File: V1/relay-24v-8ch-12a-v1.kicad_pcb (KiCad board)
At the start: 2 copper layers, 98 x 67.8 mm, 47 parts, among them J1 DB141V-2.54-2P, J2 DB141V-2.54-4P, J3 DB141V-2.54-4P, J4 DB142V-5.08-4P, J5 DB142V-5.08-4P, J6 DB142V-5.08-4P, J7 DB142V-5.08-4P, K1 G5PZ-1A, K2 G5PZ-1A, K3 G5PZ-1A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

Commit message: Review before fabrication
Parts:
- R1, R2, R3, R4, R5, R6, R7, R8: value 6k8/100mW -> 10k/100mW
- moved K1 10.8 mm to (132.0, 92.8)
- moved K2 10.8 mm to (144.0, 92.8)
- moved K3 10.8 mm to (156.0, 92.8)
- moved K4 10.8 mm to (168.0, 92.8)
- moved K5 10.8 mm to (180.0, 92.8)
- moved K6 10.8 mm to (192.0, 92.8)
- moved K7 10.8 mm to (204.0, 92.8)
- moved K8 10.8 mm to (216.0, 92.8)
- moved J4 8.50 mm to (136.8, 119.0)
- moved J5 8.50 mm to (160.8, 119.0)
- moved J6 8.50 mm to (184.8, 119.0)
- moved J7 8.50 mm to (208.8, 119.0)
- moved J2 4.65 mm to (168.2, 70.5)
- moved J3 4.65 mm to (216.2, 70.5)
- moved RV1 3.25 mm to (131.5, 108.2)
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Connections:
- net Net-(D1-A) renamed /LED1
- net Net-(D1-K) renamed /IN1
- net Net-(D10-A) renamed /IN5
- net Net-(D11-A) renamed /LED6
- net Net-(D11-K) renamed /IN6
- net Net-(D13-A) renamed /LED7
- net Net-(D13-K) renamed /IN7
- net Net-(D15-A) renamed /LED8
- net Net-(D15-K) renamed /IN8
- net Net-(D3-A) renamed /LED2
- net Net-(D3-K) renamed /IN2
- net Net-(D5-A) renamed /LED3
- net Net-(D5-K) renamed /IN3
- net Net-(D7-A) renamed /LED4
- net Net-(D7-K) renamed /IN4
- net Net-(D9-A) renamed /LED5
- net Net-(J4-Pin_1) renamed /OUT1PW
- net Net-(J4-Pin_2) renamed /OUT1LD
- net Net-(J4-Pin_3) renamed /OUT2PW
- net Net-(J4-Pin_4) renamed /OUT2LD
- net Net-(J5-Pin_1) renamed /OUT3PW
- net Net-(J5-Pin_2) renamed /OUT3LD
- net Net-(J5-Pin_3) renamed /OUT4PW
- net Net-(J5-Pin_4) renamed /OUT4LD
- net Net-(J6-Pin_1) renamed /OUT5PW
- net Net-(J6-Pin_2) renamed /OUT5LD
- net Net-(J6-Pin_3) renamed /OUT6PW
- net Net-(J6-Pin_4) renamed /OUT6LD
- net Net-(J7-Pin_1) renamed /OUT7PW
- net Net-(J7-Pin_2) renamed /OUT7LD
- net Net-(J7-Pin_3) renamed /OUT8PW
- net Net-(J7-Pin_4) renamed /OUT8LD
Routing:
- net +24V: track 248.4 -> 238.5 mm
- net /IN6: track 53.9 -> 51.0 mm
- net /IN3: track 45.2 -> 48.0 mm
- net /IN5: track 52.4 -> 54.4 mm
- net /IN1: track 51.6 -> 53.6 mm
- net /IN7: track 47.2 -> 49.1 mm
- net /IN2: track 51.9 -> 50.0 mm
- net /IN4: track 46.9 -> 48.3 mm
- net /OUT4PW: track 48.1 -> 49.1 mm
- net /OUT8PW: track 48.1 -> 49.1 mm
- net /OUT6PW: track 48.1 -> 49.1 mm
- net /OUT2PW: track 48.1 -> 49.1 mm
- net /IN8: track 48.9 -> 49.7 mm
- net /OUT7LD: track 42.4 -> 41.7 mm
- net /OUT3LD: track 42.4 -> 41.7 mm
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- added copper zone on F.Cu, net +24V
- removed copper zone on B.Cu, net +24V
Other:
- rule pad_to_mask_clearance: 0 -> 0.1

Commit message: Revising before manufacturing.
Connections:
- net /OUT1PW renamed /OUT1LN
- net /OUT2PW renamed /OUT2LN
- net /OUT3PW renamed /OUT3LN
- net /OUT4PW renamed /OUT4LN
- net /OUT5PW renamed /OUT5LN
- net /OUT6PW renamed /OUT6LN
- net /OUT7PW renamed /OUT7LN
- net /OUT8PW renamed /OUT8LN
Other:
- board text added: "LINE"
- board text removed: "V~"
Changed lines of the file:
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@@
 	(net 17 "/IN8")
 	(net 18 "/OUT1LD")
-	(net 19 "/OUT2PW")
+	(net 19 "/OUT2LN")
 	(net 20 "/OUT2LD")
-	(net 21 "/OUT1PW")
+	(net 21 "/OUT1LN")
 	(net 22 "/OUT3LD")
-	(net 23 "/OUT4PW")
+	(net 23 "/OUT4LN")
 	(net 24 "/OUT4LD")
-	(net 25 "/OUT3PW")
-	(net 26 "/OUT5PW")
+	(net 25 "/OUT3LN")
+	(net 26 "/OUT5LN")
 	(net 27 "/OUT6LD")
-	(net 28 "/OUT6PW")
+	(net 28 "/OUT6LN")
 	(net 29 "/OUT5LD")
-	(net 30 "/OUT7PW")
+	(net 30 "/OUT7LN")
 	(net 31 "/OUT8LD")
-	(net 32 "/OUT8PW")
+	(net 32 "/OUT8LN")
 	(net 33 "/OUT7LD")
 	(footprint "Tales:D_SOD-123"
@@
 			(layers "*.Cu" "*.Mask")
 			(remove_unused_layers no)
-			(net 23 "/OUT4PW")
+			(net 23 "/OUT4LN")
 			(pintype "passive")
 		)
@@
 			(layers "*.Cu" "*.Mask")
 			(remove_unused_layers no)
-			(net 21 "/OUT1PW")
+			(net 21 "/OUT1LN")
 			(pintype "passive")
 		)
@@
 			(layers "*.Cu" "*.Mask")
 			(remove_unused_layers no)
-			(net 28 "/OUT6PW")
+			(net 28 "/OUT6LN")
 			(pintype "passive")
 		)
@@
 			(layers "*.Cu" "*.Mask")
 			(remove_unused_layers no)
-			(net 26 "/OUT5PW")
+			(net 26 "/OUT5LN")
 			(pinfunction "Pin_1")
 			(pintype "passive")
@@
 			(layers "*.Cu" "*.Mask")
 			(remove_unused_layers no)
-			(net 26 "/OUT5PW")
+			(net 26 "/OUT5LN")
 			(pinfunction "Pin_1")
 			(pintype "passive")
@@
 			(layers "*.Cu" "*.Mask")
 			(remove_unused_layers no)
-			(net 28 "/OUT6PW")
+			(net 28 "/OUT6LN")
 			(pinfunction "Pin_3")
 			(pintype "passive")
@@
 			(layers "*.Cu" "*.Mask")
 			(remove_unused_layers no)
-			(net 28 "/OUT6PW")
+			(net 28 "/OUT6LN")
 			(pinfunction "Pin_3")
 			(pintype "passive")
@@
 			(layers "*.Cu" "*.Mask")
 			(remove_unused_layers no)
-			(net 30 "/OUT7PW")
+			(net 30 "/OUT7LN")
 			(pintype "passive")
 		)
@@
 			(layers "*.Cu" "*.Mask")
 			(remove_unused_layers no)
-			(net 28 "/OUT6PW")
+			(net 28 "/OUT6LN")
 			(pintype "passive")
 		)
@@
 			(layers "*.Cu" "*.Mask")
 			(remove_unused_layers no)
-			(net 32 "/OUT8PW")
+			(net 32 "/OUT8LN")
 			(pintype "passive")
 		)
@@
 			(layers "*.Cu" "*.Mask")
 			(remove_unused_layers no)
-			(net 25 "/OUT3PW")
+			(net 25 "/OUT3LN")
 			(pintype "passive")
 		)
@@
 			(layers "*.Cu" "*.Mask")
 			(remove_unused_layers no)
-			(net 26 "/OUT5PW")
+			(net 26 "/OUT5LN")
 			(pintype "passive")
 		)
@@
 			(layers "*.Cu" "*.Mask")
 			(remove_unused_layers no)
-			(net 23 "/OUT4PW")
+			(net 23 "/OUT4LN")
 			(pintype "passive")
 		)
@@
 			(layers "*.Cu" "*.Mask")
 			(remove_unused_layers no)
-			(net 19 "/OUT2PW")
+			(net 19 "/OUT2LN")
 			(pintype "passive")
 		)
@@
 			(layers "*.Cu" "*.Mask")
 			(remove_unused_layers no)
-			(net 32 "/OUT8PW")
+			(net 32 "/OUT8LN")
 			(pintype "passive")
 		)
@@
 			(layers "*.Cu" "*.Mask")
 			(remove_unused_layers no)
-			(net 19 "/OUT2PW")
+			(net 19 "/OUT2LN")
 			(pintype "passive")
 		)
@@
 			(layers "*.Cu" "*.Mask")
 			(remove_unused_layers no)
-			(net 30 "/OUT7PW")
+			(net 30 "/OUT7LN")
 			(pinfunction "Pin_1")
 			(pintype "passive")
@@
 			(layers "*.Cu" "*.Mask")
 			(remove_unused_layers no)
-			(net 30 "/OUT7PW")
+			(net 30 "/OUT7LN")
 			(pinfunction "Pin_1")
 			(pintype "passive")
@@
 			(layers "*.Cu" "*.Mask")
 			(remove_unused_layers no)
-			(net 32 "/OUT8PW")
+			(net 32 "/OUT8LN")
 			(pinfunction "Pin_3")
 			(pintype "passive")
@@
 			(layers "*.Cu" "*.Mask")
 			(remove_unused_layers no)
-			(net 32 "/OUT8PW")
+			(net 32 "/OUT8LN")
 			(pinfunction "Pin_3")
 			(pintype "passive")
@@
 			(layers "*.Cu" "*.Mask")
 			(remove_unused_layers no)
-			(net 21 "/OUT1PW")
+			(net 21 "/OUT1LN")
 			(pintype "passive")
 		)
@@
 			(layers "*.Cu" "*.Mask")
 			(remove_unused_layers no)
-			(net 21 "/OUT1PW")
+			(net 21 "/OUT1LN")
 			(pinfunction "Pin_1")
 			(pintype "passive")
@@
 			(layers "*.Cu" "*.Mask")
 			(remove_unused_layers no)
-			(net 21 "/OUT1PW")
+			(net 21 "/OUT1LN")
 			(pinfunction "Pin_1")
 			(pintype "passive")
@@
 			(layers "*.Cu" "*.Mask")
 			(remove_unused_layers no)
-			(net 19 "/OUT2PW")
+			(net 19 "/OUT2LN")
 			(pinfunction "Pin_3")
 			(pintype "passive")
@@
 			(layers "*.Cu" "*.Mask")
 			(remove_unused_layers no)
-			(net 19 "/OUT2PW")
+			(net 19 "/OUT2LN")
 			(pinfunction "Pin_3")
 			(pintype "passive")
@@
 			(layers "*.Cu" "*.Mask")
 			(remove_unused_layers no)
-			(net 25 "/OUT3PW")
+			(net 25 "/OUT3LN")
 			(pintype "passive")
 		)
@@
 			(layers "*.Cu" "*.Mask")
 			(remove_unused_layers no)
-			(net 25 "/OUT3PW")
+			(net 25 "/OUT3LN")
 			(pinfunction "Pin_1")
 			(pintype "passive")
@@
 			(layers "*.Cu" "*.Mask")
 			(remove_unused_layers no)
-			(net 25 "/OUT3PW")
+			(net 25 "/OUT3LN")
 			(pinfunction "Pin_1")
 			(pintype "passive")
@@
 			(layers "*.Cu" "*.Mask")
 			(remove_unused_layers no)
-			(net 23 "/OUT4PW")
+			(net 23 "/OUT4LN")
 			(pinfunction "Pin_3")
 			(pintype "passive")
@@
 			(layers "*.Cu" "*.Mask")
 			(remove_unused_layers no)
-			(net 23 "/OUT4PW")
+			(net 23 "/OUT4LN")
 			(pinfunction "Pin_3")
 			(pintype "passive")
@@
 			(layers "*.Cu" "*.Mask")
 			(remove_unused_layers no)
-			(net 26 "/OUT5PW")
+			(net 26 "/OUT5LN")
 			(pintype "passive")
 		)
@@
 			(layers "*.Cu" "*.Mask")
 			(remove_unused_layers no)
-			(net 30 "/OUT7PW")
+			(net 30 "/OUT7LN")
 			(pintype "passive")
 		)
@@
 		)
 	)
-	(gr_text "V~"
+	(gr_text "LINE"
 		(at 187.26 125.75 0)
 		(layer "F.SilkS")
@@
 		)
 	)
-	(gr_text "V~"
+	(gr_text "LINE"
 		(at 139.26 125.75 0)
 		(layer "F.SilkS")
@@
 		)
 	)
-	(gr_text "V~"
+	(gr_text "LINE"
 		(at 163.16 125.75 0)
 		(layer "F.SilkS")
@@
 		)
 	)
-	(gr_text "V~"
+	(gr_text "LINE"
 		(at 129.1 125.75 0)
 		(layer "F.SilkS")
@@
 		)
 	)
-	(gr_text "V~"
+	(gr_text "LINE"
 		(at 211.16 125.75 0)
 		(layer "F.SilkS")
@@
 		)
 	)
-	(gr_text "V~"
+	(gr_text "LINE"
 		(at 201 125.75 0)
 		(layer "F.SilkS")
@@
 		)
 	)
-	(gr_text "V~"
+	(gr_text "LINE"
 		(at 153 125.75 0)
 		(layer "F.SilkS")
@@
 		)
 	)
-	(gr_text "V~"
+	(gr_text "LINE"
 		(at 177.1 125.75 0)
 		(layer "F.SilkS")

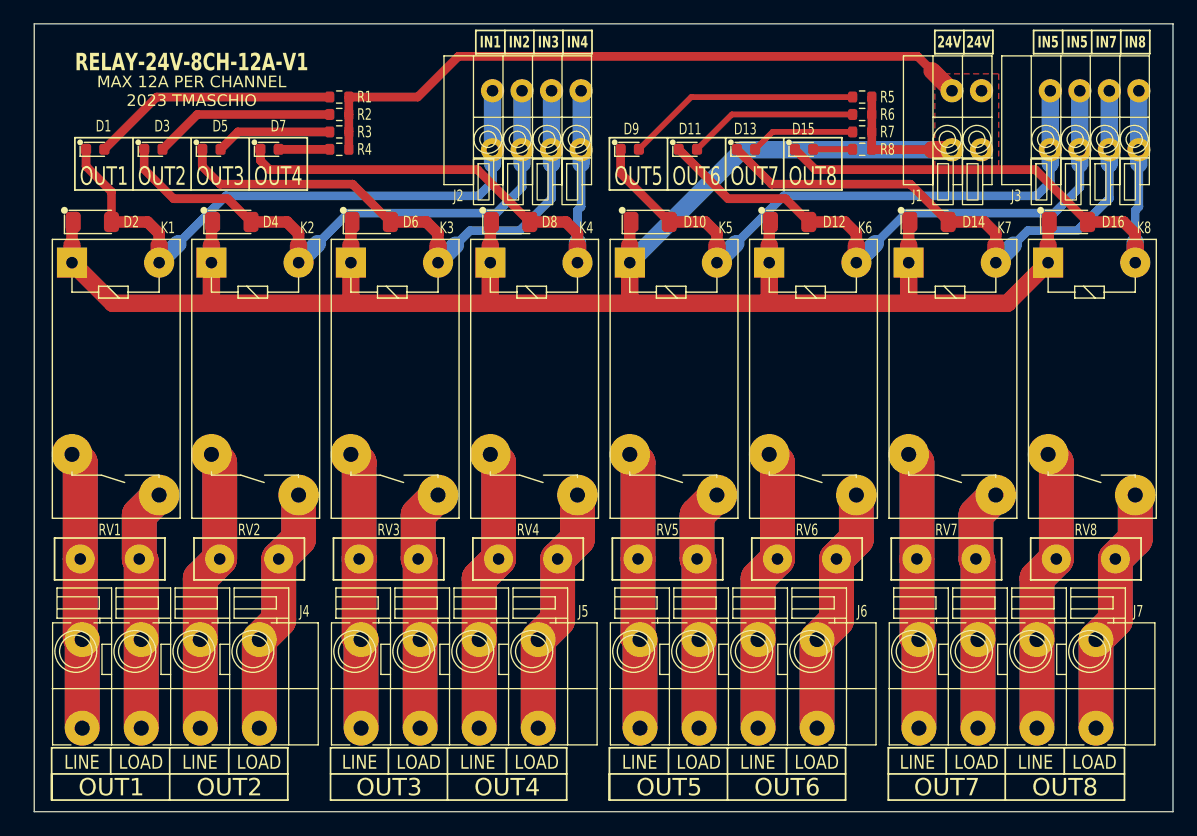
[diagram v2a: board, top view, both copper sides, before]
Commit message: Replaced input terminal blocks for 3.5mm pitch.
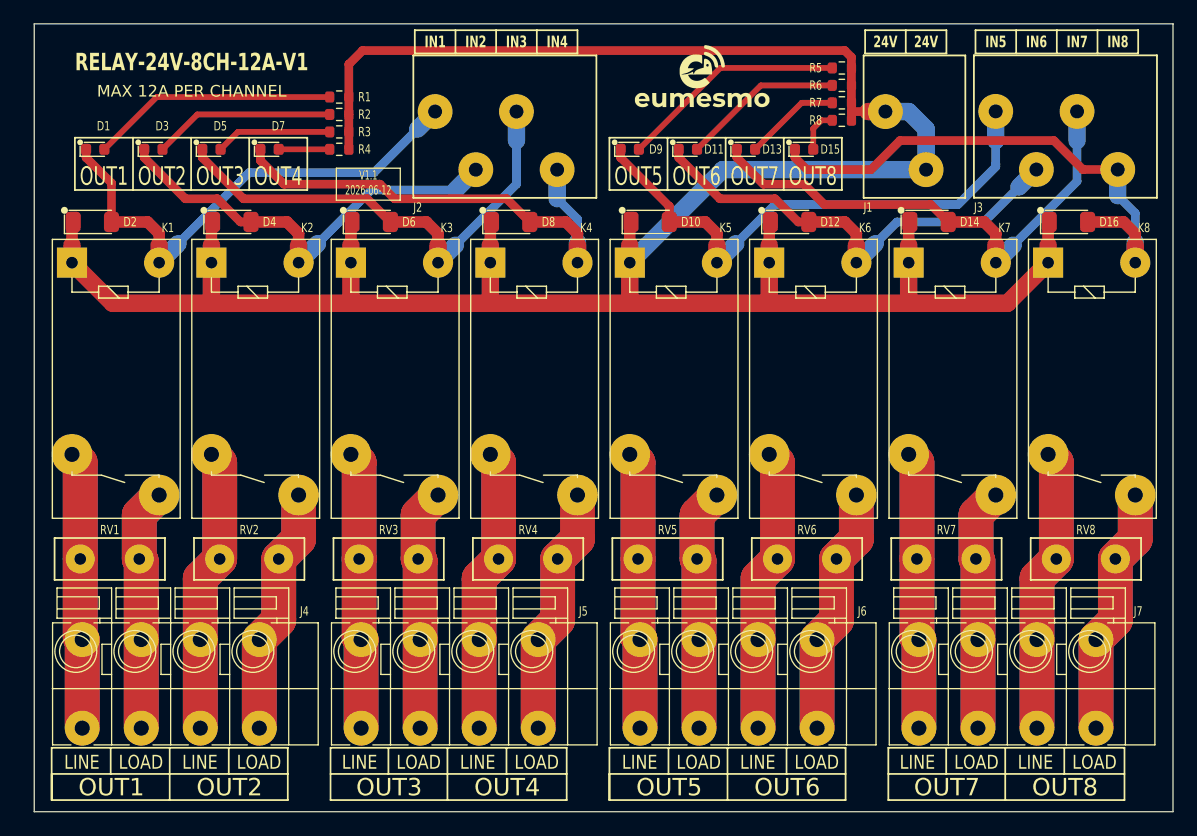
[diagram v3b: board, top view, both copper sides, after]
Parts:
- added G***: LOGO, Tales:Eumesmo_small_silk, F.Cu at (182.5, 66.8)
- J1: value DB141V-2.54-2P -> 250-202; footprint Tales:TerminalBlock_Dibo_DB141V-2.54-2P_1x02_P2.54mm_Vertical -> Tales:TerminalBlock_Wago_250-202_1x02_P3.5mm_45Degree
- J2, J3: value DB141V-2.54-4P -> 250-204; footprint Tales:TerminalBlock_Dibo_DB141V-2.54-4P_1x04_P2.54mm_Vertical -> Tales:TerminalBlock_Wago_250-204_1x04_P3.5mm_45Degree
- moved J1 5.53 mm to (200.0, 72.2)
- moved J2 3.91 mm to (164.8, 72.2)
- moved J3 3.69 mm to (213.0, 72.2)
- moved R5 3.05 mm to (194.5, 66.0)
- moved R6 3.05 mm to (194.5, 67.5)
- moved R7 3.05 mm to (194.5, 69.0)
- moved R8 3.05 mm to (194.5, 70.5)
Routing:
- net /IN2: track 50.0 -> 37.8 mm
- net /IN6: track 51.0 -> 40.0 mm
- net /IN1: track 53.6 -> 43.3 mm
- net +24V: track 238.5 -> 231.2 mm
- net /IN5: track 54.4 -> 47.2 mm
- net /IN4: track 48.3 -> 42.1 mm
- net /IN3: track 48.0 -> 42.0 mm
- net /IN7: track 49.1 -> 44.1 mm
- net /IN8: track 49.7 -> 46.6 mm
- net /LED7: track 9.01 -> 8.29 mm
- net /LED6: track 14.6 -> 13.9 mm
- net /LED5: track 20.3 -> 19.5 mm
- removed copper zone on F.Cu, net +24V
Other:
- board text added: "IN6"
- board text added: "MAX 12A PER CHANNEL"
- board text added: "V1.1 2026-06-12"
- board text removed: "MAX 12A PER CHANNEL 2023 TMASCHIO"
